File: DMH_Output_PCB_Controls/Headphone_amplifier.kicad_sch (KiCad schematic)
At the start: 24 parts, among them U11 TL074, U12 NE5532, U13 NE5532, U14 NE5532, U15 NE5532

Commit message: Starting Controls PCB design
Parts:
- added J12: Conn_01x06, Connector_PinSocket_2.54mm:PinSocket_1x06_P2.54mm_Vertical, symbol Connector_Generic:Conn_01x06
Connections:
- net L_Monitor: now also J12.3 (Pin_3)
- net R_Monitor: now also J12.6 (Pin_6)
- net at RV2.5, U11.12 (+): now also J12.5 (Pin_5)
- net at C13.2, R44.2, R48.1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: now also J12.1 (Pin_1)
- net at RV2.2, U11.3 (+): now also J12.2 (Pin_2)
- net at C14.2, R46.2, R57.1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: now also J12.4 (Pin_4)

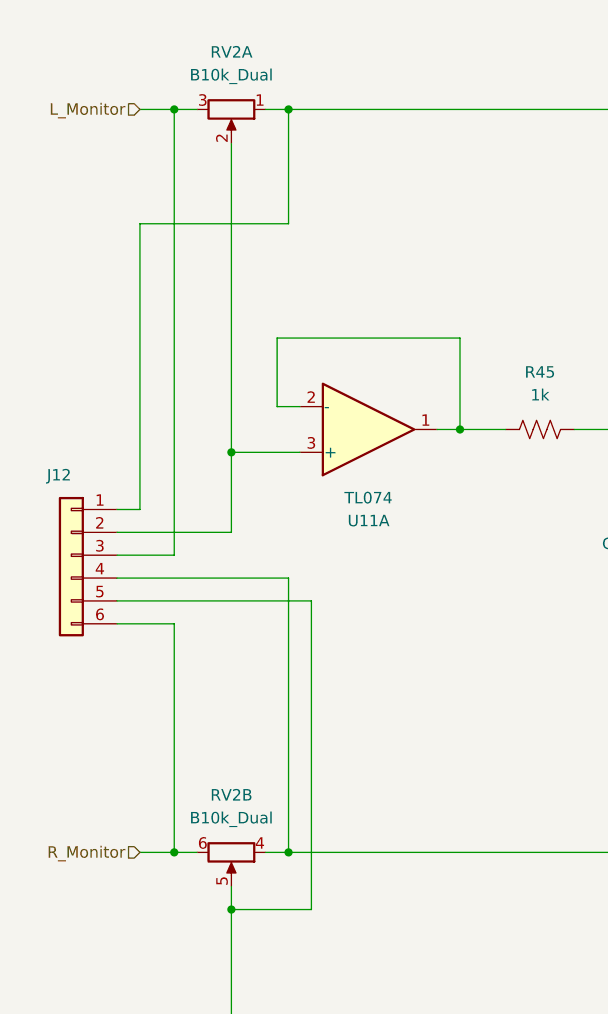
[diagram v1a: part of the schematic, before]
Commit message: Controls PCB placement ongoing
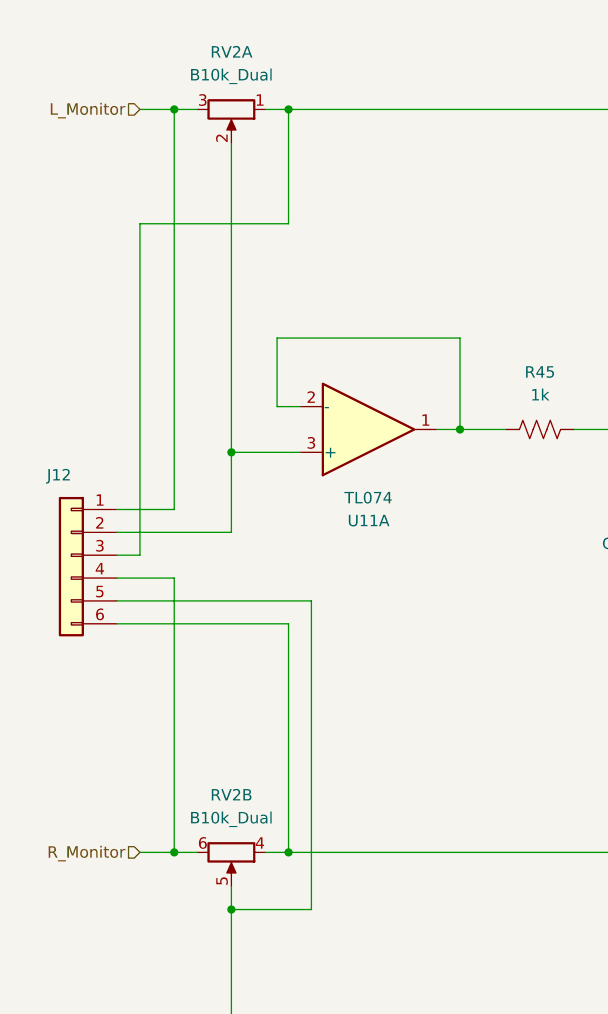
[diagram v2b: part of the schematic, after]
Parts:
- RV2: Function (none) -> HP Volume
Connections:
- net L_Monitor: now also J12.1 (Pin_1); no longer J12.3 (Pin_3)
- net R_Monitor: now also J12.4 (Pin_4); no longer J12.6 (Pin_6)
- net at C13.2, R44.2, R48.1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: now also J12.3 (Pin_3); no longer J12.1 (Pin_1)
- net at C14.2, R46.2, R57.1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: now also J12.6 (Pin_6); no longer J12.4 (Pin_4)
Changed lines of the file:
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@@
 	(wire
 		(pts
-			(xy 29.21 74.93) (xy 29.21 25.4)
+			(xy 29.21 69.85) (xy 29.21 25.4)
 		)
 		(stroke
@@
 	(wire
 		(pts
+			(xy 22.86 69.85) (xy 29.21 69.85)
+		)
+		(stroke
+			(width 0)
+			(type default)
+		)
+	)
+	(wire
+		(pts
 			(xy 73.66 143.51) (xy 78.74 143.51)
 		)
@@
 	(wire
 		(pts
-			(xy 25.4 69.85) (xy 25.4 38.1)
+			(xy 25.4 74.93) (xy 22.86 74.93)
 		)
 		(stroke
@@
 	(wire
 		(pts
-			(xy 41.91 77.47) (xy 41.91 107.95)
-		)
-		(stroke
-			(width 0)
-			(type default)
-		)
-	)
-	(wire
-		(pts
 			(xy 177.8 78.74) (xy 177.8 66.04)
 		)
@@
 	(wire
 		(pts
-			(xy 22.86 69.85) (xy 25.4 69.85)
-		)
-		(stroke
-			(width 0)
-			(type default)
-		)
-	)
-	(wire
-		(pts
 			(xy 44.45 80.01) (xy 44.45 114.3)
 		)
@@
 	(wire
 		(pts
-			(xy 22.86 82.55) (xy 29.21 82.55)
-		)
-		(stroke
-			(width 0)
-			(type default)
-		)
-	)
-	(wire
-		(pts
 			(xy 137.16 76.2) (xy 137.16 66.04)
 		)
@@
 	(wire
 		(pts
-			(xy 142.24 15.24) (xy 162.56 15.24)
+			(xy 25.4 38.1) (xy 25.4 74.93)
 		)
 		(stroke
@@
 	(wire
 		(pts
-			(xy 44.45 114.3) (xy 35.56 114.3)
+			(xy 142.24 15.24) (xy 162.56 15.24)
 		)
 		(stroke
@@
 	(wire
 		(pts
-			(xy 130.81 134.62) (xy 137.16 134.62)
+			(xy 44.45 114.3) (xy 35.56 114.3)
 		)
 		(stroke
@@
 	(wire
 		(pts
-			(xy 22.86 77.47) (xy 41.91 77.47)
+			(xy 130.81 134.62) (xy 137.16 134.62)
 		)
 		(stroke
@@
 	(wire
 		(pts
-			(xy 22.86 74.93) (xy 29.21 74.93)
-		)
-		(stroke
-			(width 0)
-			(type default)
-		)
-	)
-	(wire
-		(pts
 			(xy 116.84 146.05) (xy 119.38 146.05)
 		)
@@
 	(wire
 		(pts
-			(xy 29.21 82.55) (xy 29.21 107.95)
+			(xy 177.8 161.29) (xy 177.8 148.59)
 		)
 		(stroke
@@
 	(wire
 		(pts
-			(xy 177.8 161.29) (xy 177.8 148.59)
+			(xy 43.18 140.97) (xy 40.64 140.97)
 		)
 		(stroke
@@
 	(wire
 		(pts
-			(xy 43.18 140.97) (xy 40.64 140.97)
+			(xy 40.64 133.35) (xy 60.96 133.35)
 		)
 		(stroke
@@
 	(wire
 		(pts
-			(xy 40.64 133.35) (xy 60.96 133.35)
+			(xy 160.02 161.29) (xy 162.56 161.29)
 		)
 		(stroke
@@
 	(wire
 		(pts
-			(xy 160.02 161.29) (xy 162.56 161.29)
+			(xy 162.56 173.99) (xy 162.56 161.29)
 		)
 		(stroke
@@
 	(wire
 		(pts
-			(xy 162.56 173.99) (xy 162.56 161.29)
+			(xy 29.21 77.47) (xy 29.21 107.95)
 		)
 		(stroke
@@
 	(wire
 		(pts
+			(xy 41.91 82.55) (xy 41.91 107.95)
+		)
+		(stroke
+			(width 0)
+			(type default)
+		)
+	)
+	(wire
+		(pts
 			(xy 99.06 63.5) (xy 99.06 50.8)
 		)
@@
 	(wire
 		(pts
+			(xy 22.86 82.55) (xy 41.91 82.55)
+		)
+		(stroke
+			(width 0)
+			(type default)
+		)
+	)
+	(wire
+		(pts
 			(xy 162.56 27.94) (xy 167.64 27.94)
 		)
@@
 	(wire
 		(pts
+			(xy 22.86 77.47) (xy 29.21 77.47)
+		)
+		(stroke
+			(width 0)
+			(type default)
+		)
+	)
+	(wire
+		(pts
 			(xy 162.56 119.38) (xy 162.56 132.08)
 		)
@@
 		(exclude_from_sim no)
 		(in_bom yes)
-		(on_board yes)
+		(on_board no)
 		(dnp no)
 		(fields_autoplaced yes)
@@
 		(exclude_from_sim no)
 		(in_bom yes)
-		(on_board yes)
+		(on_board no)
 		(dnp no)
 		(fields_autoplaced yes)
@@
 		(exclude_from_sim no)
 		(in_bom yes)
-		(on_board yes)
+		(on_board no)
 		(dnp no)
 		(property "Reference" "U14"
@@
 		(exclude_from_sim no)
 		(in_bom yes)
-		(on_board yes)
+		(on_board no)
 		(dnp no)
 		(property "Reference" "U13"
@@
 		(exclude_from_sim no)
 		(in_bom yes)
-		(on_board yes)
+		(on_board no)
 		(dnp no)
 		(property "Reference" "U11"
@@
 		(exclude_from_sim no)
 		(in_bom yes)
-		(on_board yes)
+		(on_board no)
 		(dnp no)
 		(property "Reference" "U14"
@@
 		(exclude_from_sim no)
 		(in_bom yes)
-		(on_board yes)
+		(on_board no)
 		(dnp no)
 		(property "Reference" "U12"
@@
 		(exclude_from_sim no)
 		(in_bom yes)
-		(on_board yes)
+		(on_board no)
 		(dnp no)
 		(property "Reference" "U12"
@@
 		(exclude_from_sim no)
 		(in_bom yes)
-		(on_board yes)
+		(on_board no)
 		(dnp no)
 		(fields_autoplaced yes)
@@
 		(exclude_from_sim no)
 		(in_bom yes)
-		(on_board yes)
+		(on_board no)
 		(dnp no)
 		(fields_autoplaced yes)
@@
 		(exclude_from_sim no)
 		(in_bom yes)
-		(on_board yes)
+		(on_board no)
 		(dnp no)
 		(property "Reference" "U15"
@@
 		(exclude_from_sim no)
 		(in_bom yes)
-		(on_board yes)
+		(on_board no)
 		(dnp no)
 		(fields_autoplaced yes)
@@
 		(exclude_from_sim no)
 		(in_bom yes)
-		(on_board yes)
+		(on_board no)
 		(dnp no)
 		(fields_autoplaced yes)
@@
 		(exclude_from_sim no)
 		(in_bom yes)
-		(on_board yes)
+		(on_board no)
 		(dnp no)
 		(fields_autoplaced yes)
@@
 		(exclude_from_sim no)
 		(in_bom yes)
-		(on_board yes)
+		(on_board no)
 		(dnp no)
 		(property "Reference" "U15"
@@
 		(exclude_from_sim no)
 		(in_bom yes)
-		(on_board yes)
+		(on_board no)
 		(dnp no)
 		(fields_autoplaced yes)
@@
 		(exclude_from_sim no)
 		(in_bom yes)
-		(on_board yes)
+		(on_board no)
 		(dnp no)
 		(property "Reference" "R56"
@@
 		(exclude_from_sim no)
 		(in_bom yes)
-		(on_board yes)
+		(on_board no)
 		(dnp no)
 		(fields_autoplaced yes)
@@
 		(exclude_from_sim no)
 		(in_bom yes)
-		(on_board yes)
+		(on_board no)
 		(dnp no)
 		(fields_autoplaced yes)
@@
 		(exclude_from_sim no)
 		(in_bom yes)
-		(on_board yes)
+		(on_board no)
 		(dnp no)
 		(property "Reference" "U11"
@@
 		(exclude_from_sim no)
 		(in_bom yes)
-		(on_board yes)
+		(on_board no)
 		(dnp no)
 		(property "Reference" "U11"
@@
 			)
 		)
-		(property "Function" ""
+		(property "Function" "HP Volume"
 			(at 35.56 107.95 0)
 			(effects
 				(font
 					(size 1.27 1.27)
+					(thickness 0.254)
+					(bold yes)
+					(italic yes)
 				)
+				(hide yes)
 			)
 		)
@@
 		(exclude_from_sim no)
 		(in_bom yes)
-		(on_board yes)
+		(on_board no)
 		(dnp no)
 		(fields_autoplaced yes)
@@
 		(exclude_from_sim no)
 		(in_bom yes)
-		(on_board yes)
+		(on_board no)
 		(dnp no)
 		(fields_autoplaced yes)
@@
 		(exclude_from_sim no)
 		(in_bom yes)
-		(on_board yes)
+		(on_board no)
 		(dnp no)
 		(fields_autoplaced yes)
@@
 			)
 		)
-		(property "Function" ""
+		(property "Function" "HP Volume"
 			(at 35.56 25.4 0)
 			(effects
 				(font
 					(size 1.27 1.27)
+					(thickness 0.254)
+					(bold yes)
+					(italic yes)
 				)
+				(hide yes)
 			)
 		)
@@
 		(exclude_from_sim no)
 		(in_bom yes)
-		(on_board yes)
+		(on_board no)
 		(dnp no)
 		(fields_autoplaced yes)
@@
 		(exclude_from_sim no)
 		(in_bom yes)
-		(on_board yes)
+		(on_board no)
 		(dnp no)
 		(fields_autoplaced yes)
@@
 		(exclude_from_sim no)
 		(in_bom yes)
-		(on_board yes)
+		(on_board no)
 		(dnp no)
 		(property "Reference" "U11"
@@
 		(exclude_from_sim no)
 		(in_bom yes)
-		(on_board yes)
+		(on_board no)
 		(dnp no)
 		(fields_autoplaced yes)
@@
 		(exclude_from_sim no)
 		(in_bom yes)
-		(on_board yes)
+		(on_board no)
 		(dnp no)
 		(fields_autoplaced yes)
@@
 		(exclude_from_sim no)
 		(in_bom yes)
-		(on_board yes)
+		(on_board no)
 		(dnp no)
 		(property "Reference" "R49"
@@
 		(exclude_from_sim no)
 		(in_bom yes)
-		(on_board yes)
+		(on_board no)
 		(dnp no)
 		(fields_autoplaced yes)
@@
 		(exclude_from_sim no)
 		(in_bom yes)
-		(on_board yes)
+		(on_board no)
 		(dnp no)
 		(fields_autoplaced yes)
@@
 		(exclude_from_sim no)
 		(in_bom yes)
-		(on_board yes)
+		(on_board no)
 		(dnp no)
 		(property "Reference" "U13"
@@
 		(exclude_from_sim no)
 		(in_bom yes)
-		(on_board yes)
+		(on_board no)
 		(dnp no)
 		(fields_autoplaced yes)

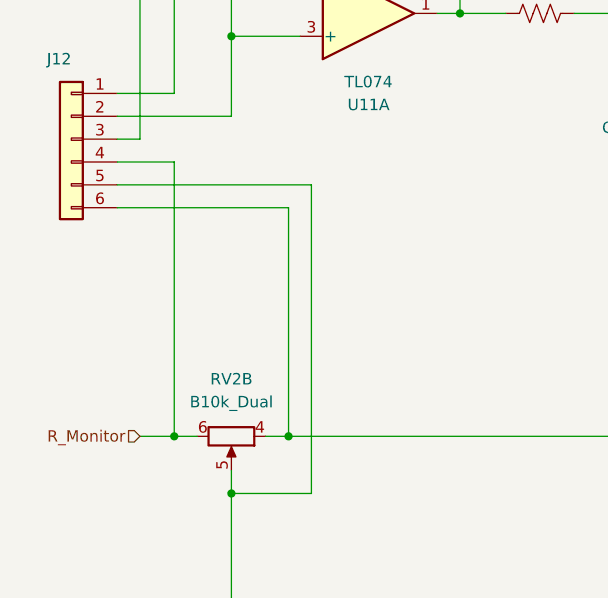
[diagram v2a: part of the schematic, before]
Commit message: Controls PCB comp placement done
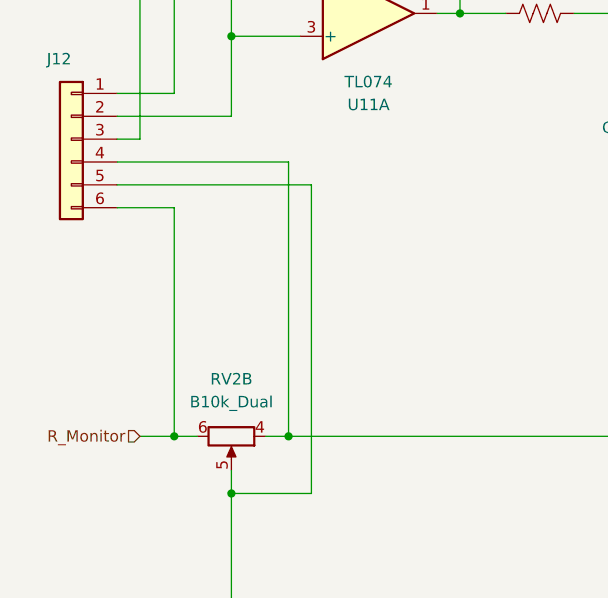
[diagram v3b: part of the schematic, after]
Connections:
- net R_Monitor: now also J12.6 (Pin_6); no longer J12.4 (Pin_4)
- net at C14.2, R46.2, R57.1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: now also J12.4 (Pin_4); no longer J12.6 (Pin_6)
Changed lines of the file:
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@@
+	(wire
+		(pts
+			(xy 22.86 82.55) (xy 29.21 82.55)
+		)
+		(stroke
+			(width 0)
+			(type default)
+		)
+	)
 	(wire
 		(pts
@@
 	(wire
 		(pts
+			(xy 22.86 77.47) (xy 41.91 77.47)
+		)
+		(stroke
+			(width 0)
+			(type default)
+		)
+	)
+	(wire
+		(pts
 			(xy 144.78 46.99) (xy 142.24 46.99)
 		)
@@
 	(wire
 		(pts
-			(xy 29.21 77.47) (xy 29.21 107.95)
+			(xy 29.21 82.55) (xy 29.21 107.95)
 		)
 		(stroke
@@
 	(wire
 		(pts
-			(xy 41.91 82.55) (xy 41.91 107.95)
+			(xy 41.91 77.47) (xy 41.91 107.95)
 		)
 		(stroke
@@
 	(wire
 		(pts
-			(xy 22.86 82.55) (xy 41.91 82.55)
-		)
-		(stroke
-			(width 0)
-			(type default)
-		)
-	)
-	(wire
-		(pts
 			(xy 162.56 27.94) (xy 167.64 27.94)
 		)
@@
 		)
 		(stroke
-			(width 0)
-			(type default)
-		)
-	)
-	(wire
-		(pts
-			(xy 22.86 77.47) (xy 29.21 77.47)
-		)
-		(stroke

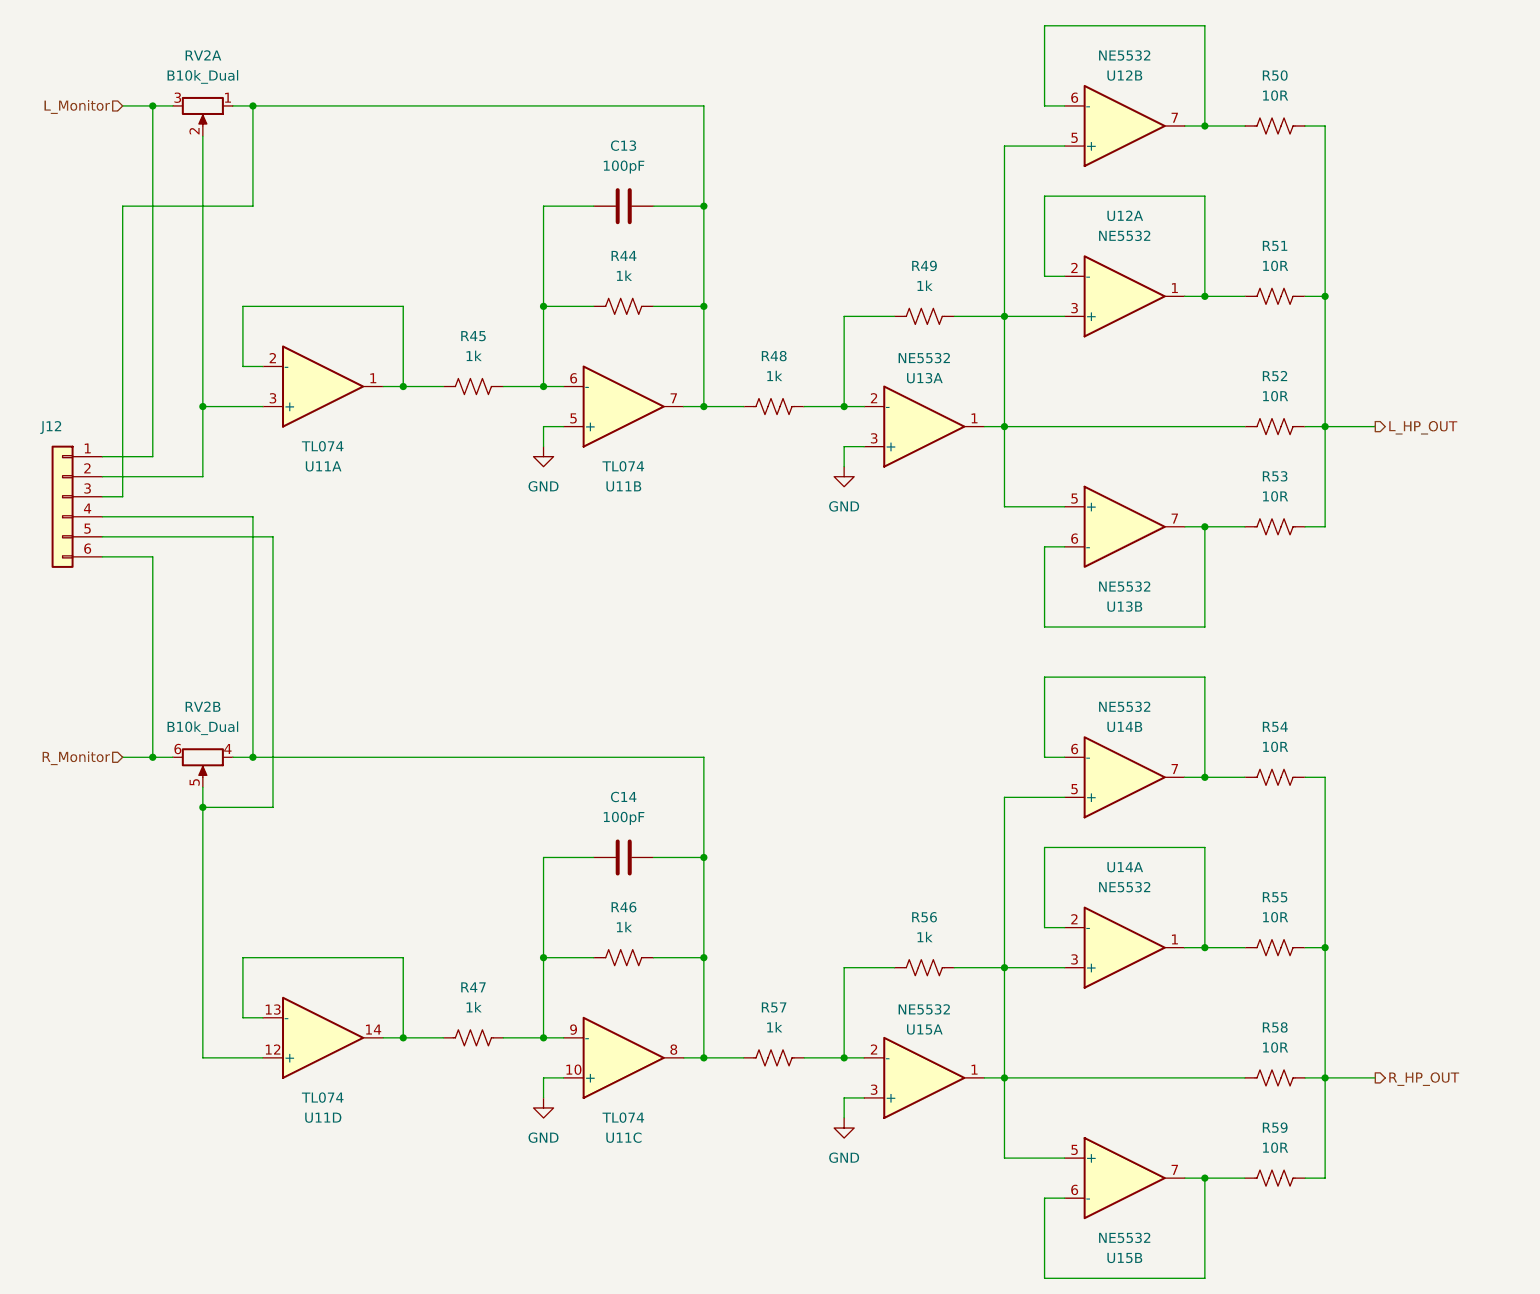
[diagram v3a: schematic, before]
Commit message: Clarified interPCB connectors in schematic
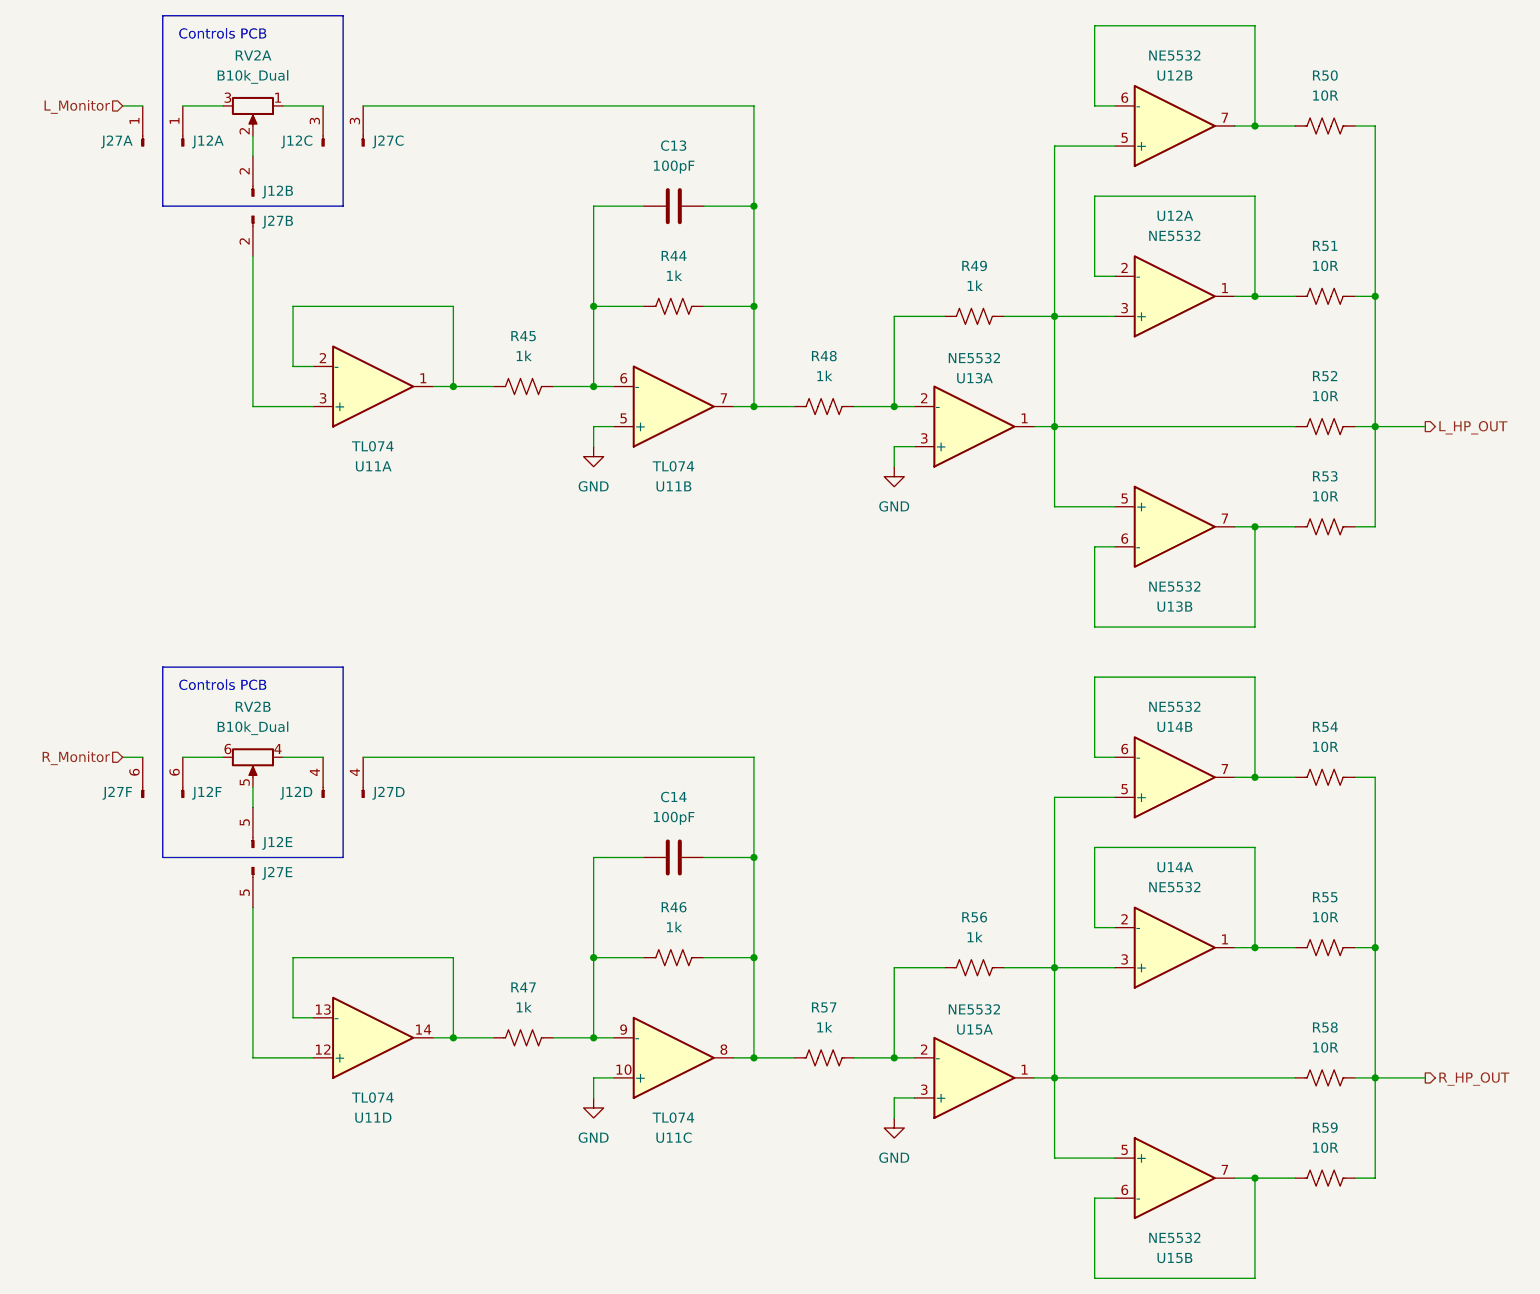
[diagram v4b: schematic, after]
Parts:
- removed J12: Conn_01x06, Connector_PinSocket_2.54mm:PinSocket_1x06_P2.54mm_Vertical, symbol Connector_Generic:Conn_01x06
- added J12: Conn_01x06_PinHeader, Connector_PinSocket_2.54mm:PinSocket_1x06_P2.54mm_Vertical, symbol SynthStuff:Conn_01x06_PinHeader
- added J27: Conn_01x06_PinHeader, Connector_PinHeader_2.54mm:PinHeader_1x06_P2.54mm_Vertical, symbol SynthStuff:Conn_01x06_PinHeader
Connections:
- net L_Monitor: now also J27.1 (Pin_1); no longer RV2.3
- net R_Monitor: now also J27.6 (Pin_6); no longer RV2.6
- net at U11.12 (+): now also J27.5 (Pin_5); no longer RV2.5
- net at C13.2, R44.2, R48.1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: now also J27.3 (Pin_3); no longer RV2.1
- net at U11.3 (+): now also J27.2 (Pin_2); no longer RV2.2
- net at C14.2, R46.2, R57.1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: now also J27.4 (Pin_4); no longer RV2.4
- new net: J12.5 (Pin_5), RV2.5
- new net: J12.1 (Pin_1), RV2.3
- new net: J12.6 (Pin_6), RV2.6
- new net: J12.3 (Pin_3), RV2.1
- new net: J12.4 (Pin_4), RV2.4
- new net: J12.2 (Pin_2), RV2.2
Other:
- note added: "Controls PCB"
- moved on the sheet: C13, C14, R44, R45, R46, R47, R48, R49, R50, R51, R52, R53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
